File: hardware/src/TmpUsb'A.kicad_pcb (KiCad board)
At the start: 2 copper layers, 25 x 17 mm, 17 parts, among them P1 48037-2200, U1 PIC18F26J50

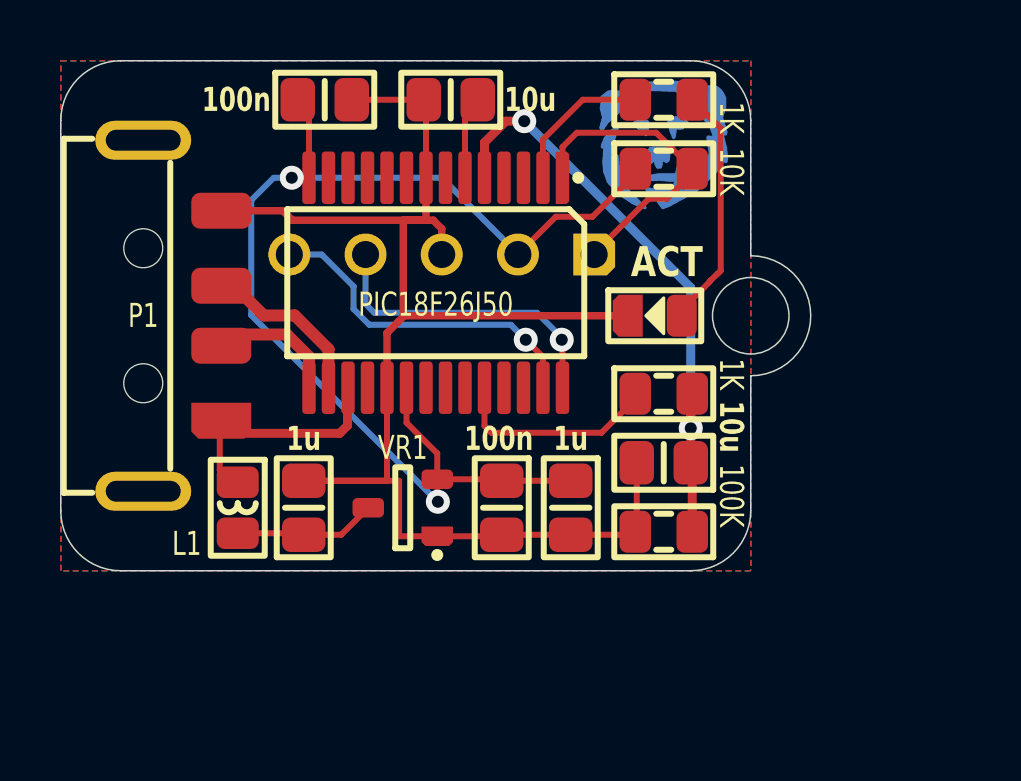
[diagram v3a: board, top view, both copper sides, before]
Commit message: Reorganizing traces a bit
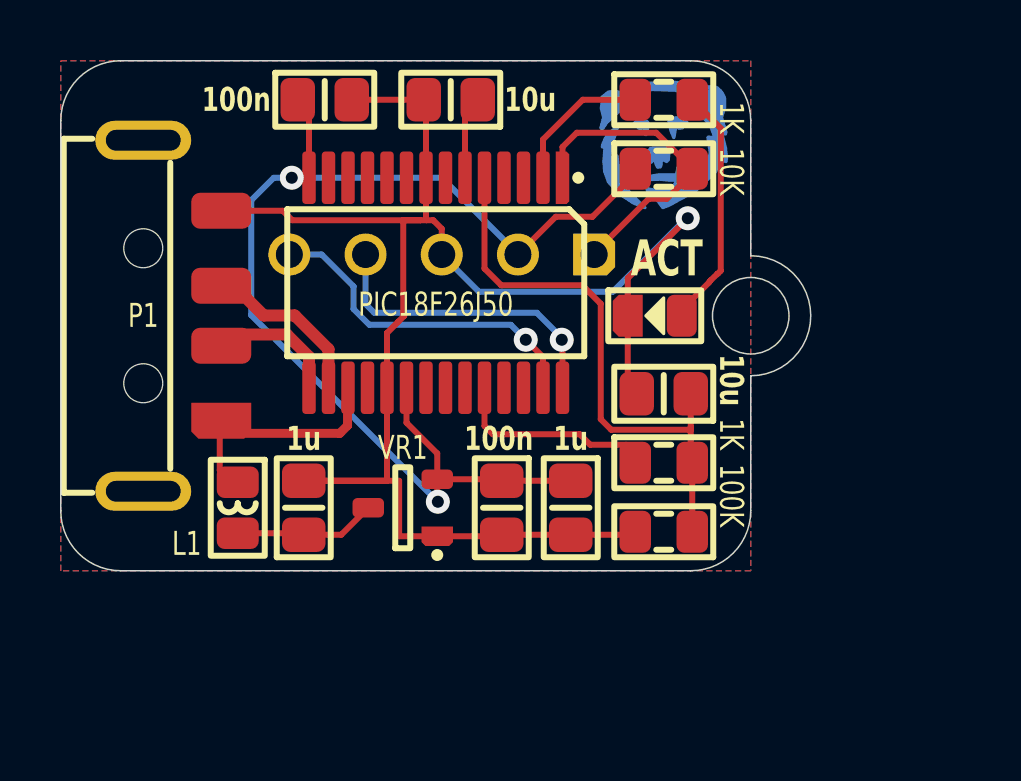
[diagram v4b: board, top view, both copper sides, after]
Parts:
- moved C6 2.30 mm to (35.1, 26.1)
- moved R2 2.30 mm to (35.1, 28.4)
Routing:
- net GND: track 49.2 -> 55.6 mm, vias 0 -> 1
- net CAP: track 20.8 -> 18.9 mm, vias 2 -> 0
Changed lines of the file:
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@@
   )
   (footprint "Medo64:C (0805)" (layer "F.Cu")
-    (at 35.1 28.4 180)
+    (at 35.1 26.1 180)
     (tags "CAPC2013X140N")
     (attr smd)
@@
         (effects (font (size 0.8 0.6) (thickness 0.15) bold))
     )
-    (fp_text value "10u" (at -2.25 1.2 270 unlocked) (layer "F.SilkS")
+    (fp_text value "10u" (at -2.25 0.45 270 unlocked) (layer "F.SilkS")
         (effects (font (size 0.8 0.6) (thickness 0.15) bold))
     )
@@
   )
   (footprint "Medo64:R (0805)" (layer "F.Cu")
-    (at 35.1 26.1)
+    (at 35.1 28.4)
     (tags "RESC2013X70N")
     (attr smd)
@@
         (effects (font (size 0.8 0.6) (thickness 0.15)))
     )
-    (fp_text value "1K" (at 2.25 -0.65 -90 unlocked) (layer "F.SilkS")
+    (fp_text value "1K" (at 2.25 -0.95 -90 unlocked) (layer "F.SilkS")
         (effects (font (size 0.8 0.6) (thickness 0.15)))
     )
@@
   )
   (gr_text "ACT" (at 34 22.3) (layer "F.SilkS" knockout)
-    (effects (font (size 1 0.8) (thickness 0.2) bold) (justify left bottom))
+    (effects (font (size 1.2 0.8) (thickness 0.2) bold) (justify left bottom))
   )
   (segment (start 23.925 24.615) (end 22.801 23.491) (width 0.4) (layer "F.Cu") (net 1))
@@
   (segment (start 22.536 24.126) (end 23.275 24.865) (width 0.4) (layer "F.Cu") (net 2))
   (segment (start 32 30.8) (end 34.05 30.8) (width 0.2) (layer "F.Cu") (net 3))
-  (segment (start 27.7 21.459) (end 27.7 20.6) (width 0.25) (layer "F.Cu") (net 3))
-  (segment (start 27.416 20.316) (end 27.192 20.316) (width 0.25) (layer "F.Cu") (net 3))
+  (segment (start 27.7 21.459) (end 27.7 20.6) (width 0.2) (layer "F.Cu") (net 3))
+  (segment (start 27.416 20.316) (end 27.192 20.316) (width 0.2) (layer "F.Cu") (net 3))
   (segment (start 27.175 18.5) (end 27.175 16.375) (width 0.2) (layer "F.Cu") (net 3))
-  (segment (start 22.716 20.316) (end 22.4 20) (width 0.25) (layer "F.Cu") (net 3))
+  (segment (start 22.716 20.316) (end 22.4 20) (width 0.2) (layer "F.Cu") (net 3))
   (segment (start 26.28 30.85) (end 27.55 30.85) (width 0.2) (layer "F.Cu") (net 3))
-  (segment (start 33.9 23.5) (end 26.45 23.5) (width 0.25) (layer "F.Cu") (net 3))
-  (segment (start 25.875 25.9) (end 25.875 24.075) (width 0.25) (layer "F.Cu") (net 3))
+  (segment (start 25.875 25.9) (end 25.875 24.075) (width 0.2) (layer "F.Cu") (net 3))
   (segment (start 25.875 29) (end 23.1 29) (width 0.2) (layer "F.Cu") (net 3))
   (segment (start 25.875 25.9) (end 25.875 29) (width 0.2) (layer "F.Cu") (net 3))
+  (segment (start 33.9 22.25) (end 35.9 20.25) (width 0.2) (layer "F.Cu") (net 3))
   (segment (start 23.1 29) (end 26.28 29) (width 0.2) (layer "F.Cu") (net 3))
-  (segment (start 25.875 24.075) (end 26.25 23.7) (width 0.25) (layer "F.Cu") (net 3))
+  (segment (start 25.875 24.075) (end 26.25 23.7) (width 0.2) (layer "F.Cu") (net 3))
   (segment (start 26.28 29) (end 26.28 30.85) (width 0.2) (layer "F.Cu") (net 3))
-  (segment (start 27.192 20.316) (end 26.991 20.316) (width 0.25) (layer "F.Cu") (net 3))
-  (segment (start 27.175 20.299) (end 27.192 20.316) (width 0.25) (layer "F.Cu") (net 3))
-  (segment (start 26.416637 23.466637) (end 26.45 23.5) (width 0.25) (layer "F.Cu") (net 3))
-  (segment (start 27.175 18.9) (end 27.175 20.299) (width 0.25) (layer "F.Cu") (net 3))
+  (segment (start 27.192 20.316) (end 26.991 20.316) (width 0.2) (layer "F.Cu") (net 3))
+  (segment (start 27.175 20.299) (end 27.192 20.316) (width 0.2) (layer "F.Cu") (net 3))
+  (segment (start 33.9 23.5) (end 33.9 22.25) (width 0.2) (layer "F.Cu") (net 3))
+  (segment (start 26.416637 23.466637) (end 26.45 23.5) (width 0.2) (layer "F.Cu") (net 3))
+  (segment (start 27.175 18.9) (end 27.175 20.299) (width 0.2) (layer "F.Cu") (net 3))
   (segment (start 27.55 30.85) (end 29.65 30.85) (width 0.2) (layer "F.Cu") (net 3))
   (segment (start 29.7 30.8) (end 32 30.8) (width 0.2) (layer "F.Cu") (net 3))
-  (segment (start 34.2 28.4) (end 34.2 30.65) (width 0.2) (layer "F.Cu") (net 3))
-  (segment (start 22.4 20) (end 20.3 20) (width 0.25) (layer "F.Cu") (net 3))
-  (segment (start 26.45 23.5) (end 26.25 23.7) (width 0.25) (layer "F.Cu") (net 3))
-  (segment (start 26.416637 20.316) (end 26.416637 23.466637) (width 0.25) (layer "F.Cu") (net 3))
+  (segment (start 22.4 20) (end 20.3 20) (width 0.2) (layer "F.Cu") (net 3))
+  (segment (start 26.45 23.5) (end 26.25 23.7) (width 0.2) (layer "F.Cu") (net 3))
+  (segment (start 26.416637 20.316) (end 26.416637 23.466637) (width 0.2) (layer "F.Cu") (net 3))
   (segment (start 27.1 16.3) (end 24.7 16.3) (width 0.2) (layer "F.Cu") (net 3))
-  (segment (start 26.991 20.316) (end 22.716 20.316) (width 0.25) (layer "F.Cu") (net 3))
-  (segment (start 27.7 20.6) (end 27.416 20.316) (width 0.25) (layer "F.Cu") (net 3))
-  (segment (start 26.991 20.316) (end 26.416637 20.316) (width 0.25) (layer "F.Cu") (net 3))
-  (segment (start 36 28.4) (end 36 26.15) (width 0.3) (layer "F.Cu") (net 4))
-  (segment (start 36 27.2) (end 36 26.15) (width 0.3) (layer "F.Cu") (net 4))
-  (segment (start 29.125 17.725) (end 29.125 18.9) (width 0.3) (layer "F.Cu") (net 4))
-  (segment (start 36.05 30.7) (end 36.05 28.45) (width 0.3) (layer "F.Cu") (net 4))
-  (segment (start 29.836 17.014) (end 29.125 17.725) (width 0.3) (layer "F.Cu") (net 4))
-  (segment (start 30.45 17.014) (end 29.836 17.014) (width 0.3) (layer "F.Cu") (net 4))
-  (via (at 36 27.25) (size 0.8) (drill 0.4) (layers "F.Cu" "B.Cu") (net 4))
-  (via (at 30.45 17.014) (size 0.8) (drill 0.4) (layers "F.Cu" "B.Cu") (net 4))
-  (segment (start 36 22.564) (end 36 27.2) (width 0.3) (layer "B.Cu") (net 4))
-  (segment (start 30.45 17.014) (end 36 22.564) (width 0.3) (layer "B.Cu") (net 4))
-  (segment (start 29.35 27.4) (end 33.025 27.4) (width 0.2) (layer "F.Cu") (net 5))
+  (segment (start 26.991 20.316) (end 22.716 20.316) (width 0.2) (layer "F.Cu") (net 3))
+  (segment (start 27.7 20.6) (end 27.416 20.316) (width 0.2) (layer "F.Cu") (net 3))
+  (segment (start 26.991 20.316) (end 26.416637 20.316) (width 0.2) (layer "F.Cu") (net 3))
+  (segment (start 33.9 23.5) (end 33.9 25.8) (width 0.2) (layer "F.Cu") (net 3))
+  (via (at 35.9 20.25) (size 0.8) (drill 0.4) (layers "F.Cu" "B.Cu") (net 3))
+  (segment (start 35.85 20.25) (end 33.4 22.7) (width 0.2) (layer "B.Cu") (net 3))
+  (segment (start 28.941 22.7) (end 27.7 21.459) (width 0.2) (layer "B.Cu") (net 3))
+  (segment (start 35.9 20.25) (end 35.85 20.25) (width 0.2) (layer "B.Cu") (net 3))
+  (segment (start 33.4 22.7) (end 28.941 22.7) (width 0.2) (layer "B.Cu") (net 3))
+  (segment (start 29.684 22.484) (end 32.384 22.484) (width 0.2) (layer "F.Cu") (net 4))
+  (segment (start 33.35 27.3) (end 36 27.3) (width 0.2) (layer "F.Cu") (net 4))
+  (segment (start 32.384 22.484) (end 33 23.1) (width 0.2) (layer "F.Cu") (net 4))
+  (segment (start 29.125 18.9) (end 29.125 21.925) (width 0.2) (layer "F.Cu") (net 4))
+  (segment (start 33 23.1) (end 33 26.95) (width 0.2) (layer "F.Cu") (net 4))
+  (segment (start 33 26.95) (end 33.35 27.3) (width 0.2) (layer "F.Cu") (net 4))
+  (segment (start 36.05 30.7) (end 36.05 28.45) (width 0.2) (layer "F.Cu") (net 4))
+  (segment (start 29.125 21.925) (end 29.684 22.484) (width 0.2) (layer "F.Cu") (net 4))
+  (segment (start 36 27.2) (end 36 26.1) (width 0.2) (layer "F.Cu") (net 4))
+  (segment (start 36 28.4) (end 36 27.2) (width 0.2) (layer "F.Cu") (net 4))
+  (segment (start 33.85 27.8) (end 34.15 28.1) (width 0.2) (layer "F.Cu") (net 5))
+  (segment (start 29.4 27.45) (end 32.3 27.45) (width 0.2) (layer "F.Cu") (net 5))
   (segment (start 29.125 25.9) (end 29.125 27.175) (width 0.2) (layer "F.Cu") (net 5))
-  (segment (start 33.025 27.4) (end 34.15 26.275) (width 0.2) (layer "F.Cu") (net 5))
-  (segment (start 29.125 27.175) (end 29.35 27.4) (width 0.2) (layer "F.Cu") (net 5))
+  (segment (start 29.125 27.175) (end 29.4 27.45) (width 0.2) (layer "F.Cu") (net 5))
+  (segment (start 32.65 27.8) (end 33.85 27.8) (width 0.2) (layer "F.Cu") (net 5))
+  (segment (start 32.3 27.45) (end 32.65 27.8) (width 0.2) (layer "F.Cu") (net 5))
   (segment (start 36.05 18.6) (end 34.85 17.4) (width 0.2) (layer "F.Cu") (net 6))
   (segment (start 34.6 19.6) (end 35.2 19.6) (width 0.2) (layer "F.Cu") (net 6))

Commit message: Updated pogo connector
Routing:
- net CAP: track 18.9 -> 18.0 mm
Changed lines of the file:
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@@
         (effects (font (size 0.8 0.6) (thickness 0.15) bold) (justify mirror))
     )
-    (fp_text user "DAT" (at 2.54 0.9) (layer "Cmts.User")
+    (fp_text user "GND" (at 0 0.9) (layer "Cmts.User" knockout)
+        (effects (font (size 0.13 0.07) (thickness 0.01) bold))
+    )
+    (fp_text user "CLK" (at 5.08 0.9) (layer "Cmts.User" knockout)
         (effects (font (size 0.13 0.07) (thickness 0.01)))
     )
-    (fp_text user "VPP" (at -5.08 0.9) (layer "Cmts.User")
+    (fp_text user "VDD" (at -2.54 0.9) (layer "Cmts.User" knockout)
         (effects (font (size 0.13 0.07) (thickness 0.01) bold))
     )
-    (fp_text user "GND" (at 0 0.9) (layer "Cmts.User")
+    (fp_text user "DAT" (at 2.54 0.9) (layer "Cmts.User" knockout)
+        (effects (font (size 0.13 0.07) (thickness 0.01)))
+    )
+    (fp_text user "VPP" (at -5.08 0.9) (layer "Cmts.User" knockout)
         (effects (font (size 0.13 0.07) (thickness 0.01) bold))
-    )
-    (fp_text user "VDD" (at -2.54 0.9) (layer "Cmts.User")
-        (effects (font (size 0.13 0.07) (thickness 0.01) bold))
-    )
-    (fp_text user "CLK" (at 5.08 0.9) (layer "Cmts.User")
-        (effects (font (size 0.13 0.07) (thickness 0.01)))
     )
     (fp_rect (start -6.35 1.27) (end 6.35 -1.27)
@@
       )
       (stroke (width 0) (type solid)) (fill solid) (layer "B.SilkS"))
-    (pad "1" thru_hole roundrect (at -5.08 0 180) (size 1.4 1.4) (drill 0.9) (layers "*.Cu" "B.Mask") (roundrect_rratio 0.25)
+    (pad "1" thru_hole roundrect (at -5.08 0 180) (size 1.5 1.5) (drill 0.9) (layers "*.Cu" "B.Mask") (roundrect_rratio 0.25)
       (chamfer_ratio 0.2) (chamfer top_left bottom_left)
       (net 6 "ICSP_VPP"))
-    (pad "2" thru_hole circle (at -2.54 0 180) (size 1.4 1.4) (drill 0.9) (layers "*.Cu" "B.Mask")
+    (pad "2" thru_hole circle (at -2.54 0 180) (size 1.5 1.5) (drill 0.9) (layers "*.Cu" "B.Mask")
       (net 11 "+3.3V"))
-    (pad "3" thru_hole circle (at 0 0 180) (size 1.4 1.4) (drill 0.9) (layers "*.Cu" "B.Mask")
+    (pad "3" thru_hole circle (at 0 0 180) (size 1.5 1.5) (drill 0.9) (layers "*.Cu" "B.Mask")
       (net 3 "GND"))
-    (pad "4" thru_hole circle (at 2.54 0 180) (size 1.4 1.4) (drill 0.9) (layers "*.Cu" "B.Mask")
+    (pad "4" thru_hole circle (at 2.54 0 180) (size 1.5 1.5) (drill 0.9) (layers "*.Cu" "B.Mask")
       (net 13 "ICSP_PGD"))
-    (pad "5" thru_hole circle (at 5.08 0 180) (size 1.4 1.4) (drill 0.9) (layers "*.Cu" "B.Mask")
+    (pad "5" thru_hole circle (at 5.08 0 180) (size 1.5 1.5) (drill 0.9) (layers "*.Cu" "B.Mask")
       (net 14 "ICSP_PGC"))
   )
@@
   (gr_line (start 17 15) (end 36 15)
     (stroke (width 0.05) (type default)) (layer "Edge.Cuts"))
-  (gr_text "TmpUsb'A B" (at 42.352 36.238) (layer "B.SilkS")
+  (gr_text "TmpUsb'A B" (at 37.2 31.4) (layer "B.SilkS")
     (effects (font (size 1 1) (thickness 0.15)) (justify left bottom mirror))
   )
@@
   (segment (start 35.9 20.25) (end 35.85 20.25) (width 0.2) (layer "B.Cu") (net 3))
   (segment (start 33.4 22.7) (end 28.941 22.7) (width 0.2) (layer "B.Cu") (net 3))
-  (segment (start 29.684 22.484) (end 32.384 22.484) (width 0.2) (layer "F.Cu") (net 4))
   (segment (start 33.35 27.3) (end 36 27.3) (width 0.2) (layer "F.Cu") (net 4))
-  (segment (start 32.384 22.484) (end 33 23.1) (width 0.2) (layer "F.Cu") (net 4))
+  (segment (start 29.709 22.509) (end 30.89895 22.509) (width 0.2) (layer "F.Cu") (net 4))
+  (segment (start 33 24.61005) (end 33 26.95) (width 0.2) (layer "F.Cu") (net 4))
+  (segment (start 36.05 30.7) (end 36.05 28.45) (width 0.2) (layer "F.Cu") (net 4))
+  (segment (start 29.125 21.925) (end 29.709 22.509) (width 0.2) (layer "F.Cu") (net 4))
   (segment (start 29.125 18.9) (end 29.125 21.925) (width 0.2) (layer "F.Cu") (net 4))
-  (segment (start 33 23.1) (end 33 26.95) (width 0.2) (layer "F.Cu") (net 4))
+  (segment (start 30.89895 22.509) (end 33 24.61005) (width 0.2) (layer "F.Cu") (net 4))
   (segment (start 33 26.95) (end 33.35 27.3) (width 0.2) (layer "F.Cu") (net 4))
-  (segment (start 36.05 30.7) (end 36.05 28.45) (width 0.2) (layer "F.Cu") (net 4))
-  (segment (start 29.125 21.925) (end 29.684 22.484) (width 0.2) (layer "F.Cu") (net 4))
   (segment (start 36 27.2) (end 36 26.1) (width 0.2) (layer "F.Cu") (net 4))
   (segment (start 36 28.4) (end 36 27.2) (width 0.2) (layer "F.Cu") (net 4))
@@
   (via (at 30.5 24.3) (size 0.8) (drill 0.4) (layers "F.Cu" "B.Cu") (net 14))
   (segment (start 30 23.8) (end 25.284314 23.8) (width 0.2) (layer "B.Cu") (net 14))
+  (segment (start 23.659 21.459) (end 22.62 21.459) (width 0.2) (layer "B.Cu") (net 14))
   (segment (start 25.284314 23.8) (end 24.76 23.275685) (width 0.2) (layer "B.Cu") (net 14))
+  (segment (start 24.76 22.56) (end 23.659 21.459) (width 0.2) (layer "B.Cu") (net 14))
   (segment (start 30.58 24.38) (end 30 23.8) (width 0.2) (layer "B.Cu") (net 14))
-  (segment (start 23.6995 21.459) (end 22.62 21.459) (width 0.2) (layer "B.Cu") (net 14))
-  (segment (start 24.76 22.5195) (end 23.6995 21.459) (width 0.2) (layer "B.Cu") (net 14))
-  (segment (start 24.76 23.275685) (end 24.76 22.5195) (width 0.2) (layer "B.Cu") (net 14))
+  (segment (start 24.76 23.275685) (end 24.76 22.56) (width 0.2) (layer "B.Cu") (net 14))
   (zone (net 3) (net_name "GND") (layers "F&B.Cu") (hatch none 0.5)
     (connect_pads (clearance 0.3))

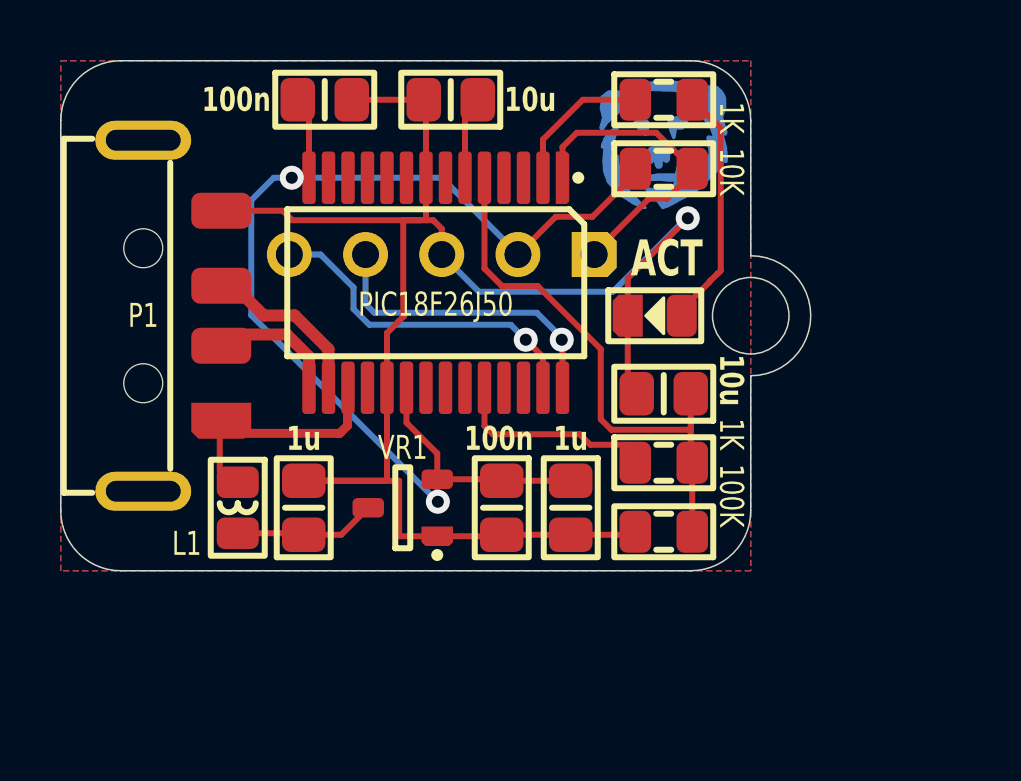
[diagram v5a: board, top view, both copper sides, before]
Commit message: Updating footprints
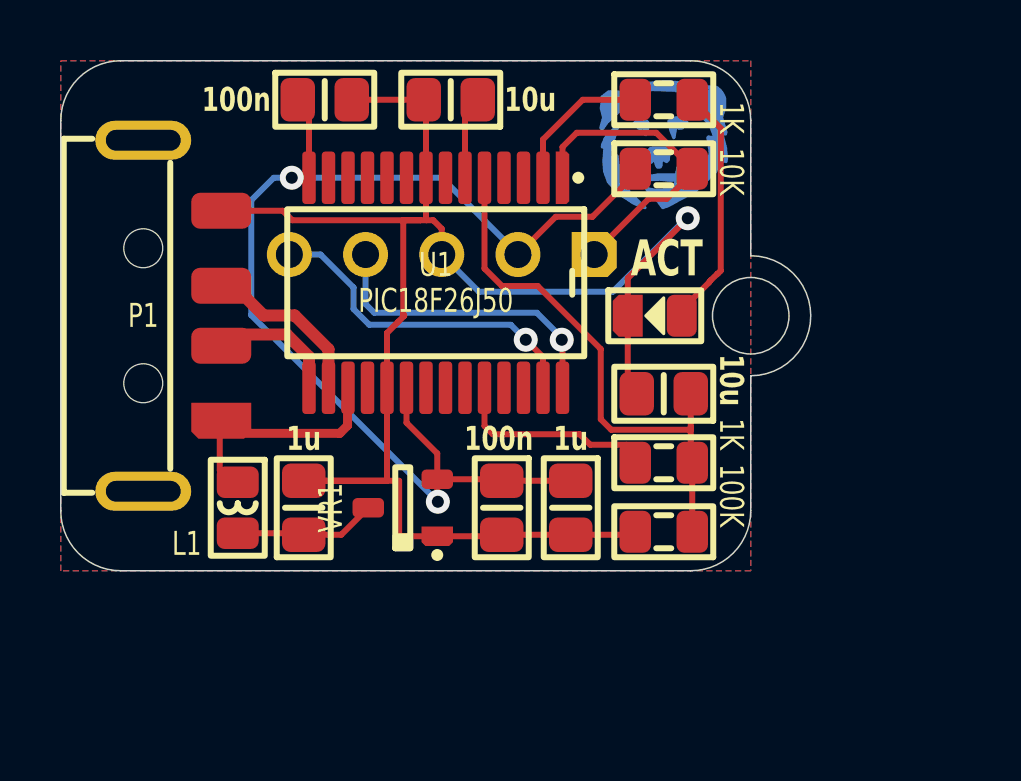
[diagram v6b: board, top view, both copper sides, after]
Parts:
- U1: footprint Medo64:U Micro PIC18F26J50 (SSOP-28) -> Medo64:U Micro [PIC18F26J50] (SSOP-28)
- VR1: footprint Medo64:VR Linear MCP1700 (SOT23-3) -> Medo64:VR Linear 3.3V 250mA [MCP1700] (SOT-23)
